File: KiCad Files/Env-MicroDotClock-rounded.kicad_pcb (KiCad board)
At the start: 2 copper layers, 90 x 65.2 mm, 47 parts, among them IC1 IS31FL3730-QFLS2-TR, IC2 IS31FL3730-QFLS2-TR, IC3 IS31FL3730-QFLS2-TR, IC4 IS31FL3730-QFLS2-TR, M1 Dip-14 Socket, M2 Dip-14 Socket, M3 Dip-14 Socket, M4 Dip-14 Socket, M5 Dip-14 Socket, M6 Dip-14 Socket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

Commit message: ru version
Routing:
- net IC3C8: track 25.3 -> 20.7 mm
- net IC3C4: track 37.9 -> 37.0 mm
- net +3V3: track 252.1 -> 253.0 mm
- net IC3C6: track 22.1 -> 21.3 mm
- net IC3C3: track 38.7 -> 38.1 mm

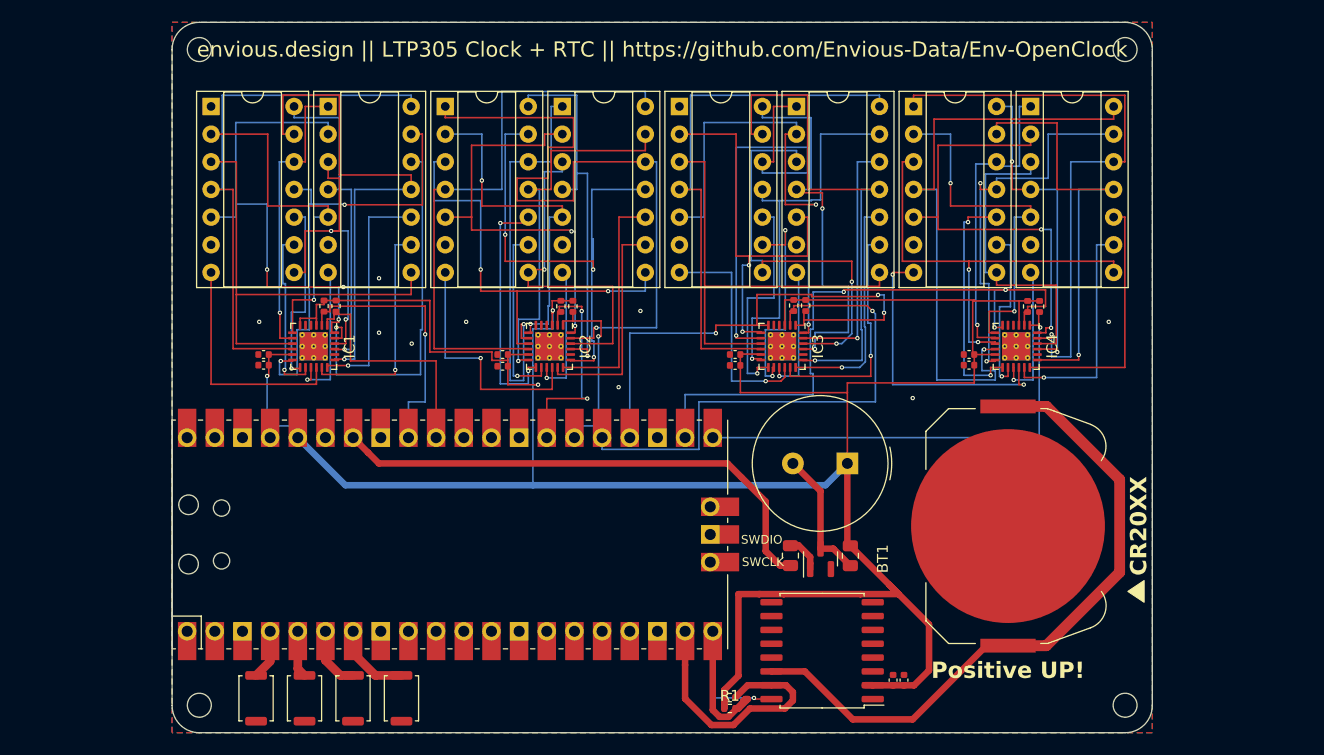
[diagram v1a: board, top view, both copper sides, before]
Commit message: Added ability to set time and show date!
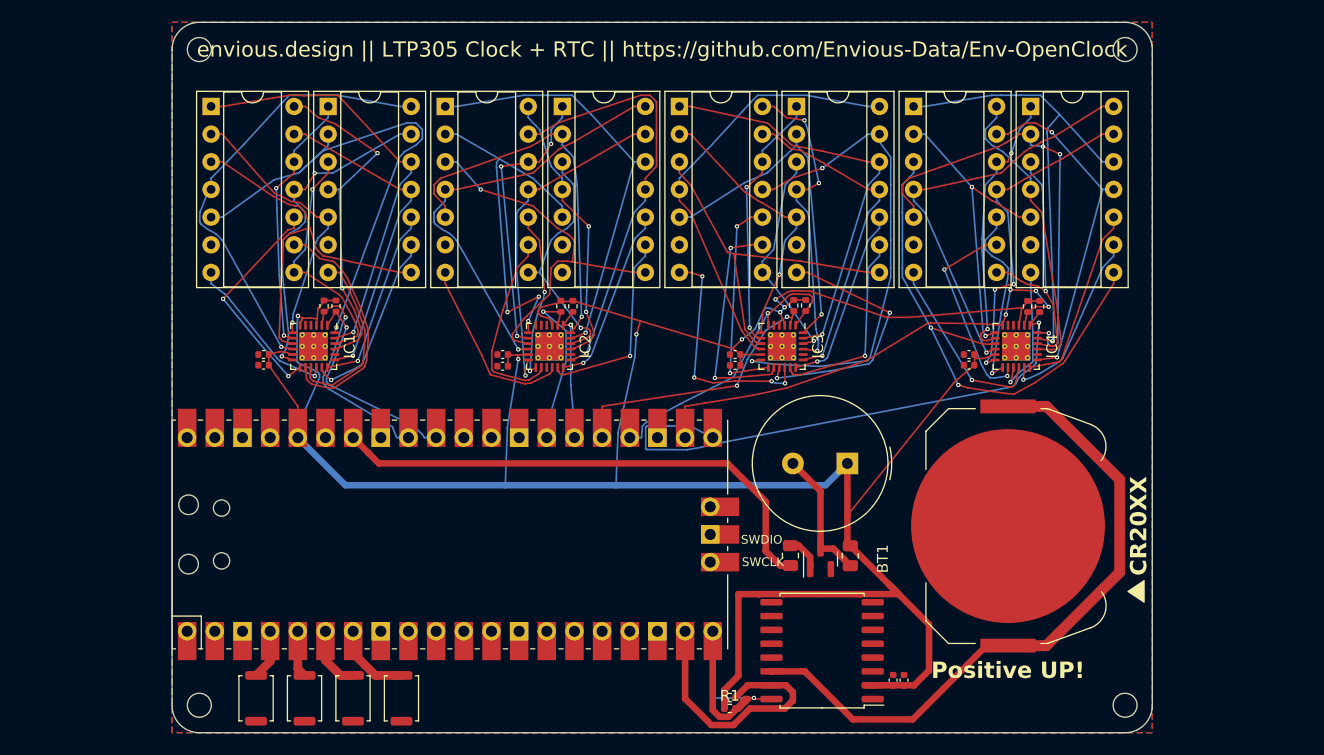
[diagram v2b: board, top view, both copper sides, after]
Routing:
- net IC2C2: track 66.1 -> 38.9 mm
- net I2C3_SCL: track 48.5 -> 25.3 mm, vias 1 -> 2
- net I2C3_SDA: track 49.8 -> 27.4 mm, vias 3 -> 1
- net IC4R4: track 56.2 -> 37.9 mm
- net IC3R2: track 42.1 -> 23.8 mm, vias 1 -> 2
- net IC3C3: track 38.1 -> 20.0 mm, vias 2 -> 1
- net IC3C5: track 47.9 -> 30.4 mm
- net IC1C5: track 47.7 -> 30.2 mm
- net IC3C2: track 23.2 -> 38.2 mm
- net IC2R4: track 53.1 -> 39.0 mm, vias 0 -> 1
- net I2C4_SCL: track 57.8 -> 44.5 mm, vias 3 -> 4
- net IC2R8: track 12.8 -> 0.00 mm, vias 1 -> 0
- net IC2R2: track 38.5 -> 26.6 mm, vias 1 -> 3
- net IC3R1: track 36.9 -> 25.1 mm, vias 2 -> 1
- net IC3R8: track 12.3 -> 24.1 mm, vias 1 -> 2
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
